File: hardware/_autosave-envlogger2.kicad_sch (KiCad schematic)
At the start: 20 parts, among them J1 Conn_01x06_Pin, J2 Conn_01x03_Socket, J3 Conn_01x03_Socket, SW1 SW_Push, U1 STM32L432KCUx, U2 BME280, Y1 32 kHz

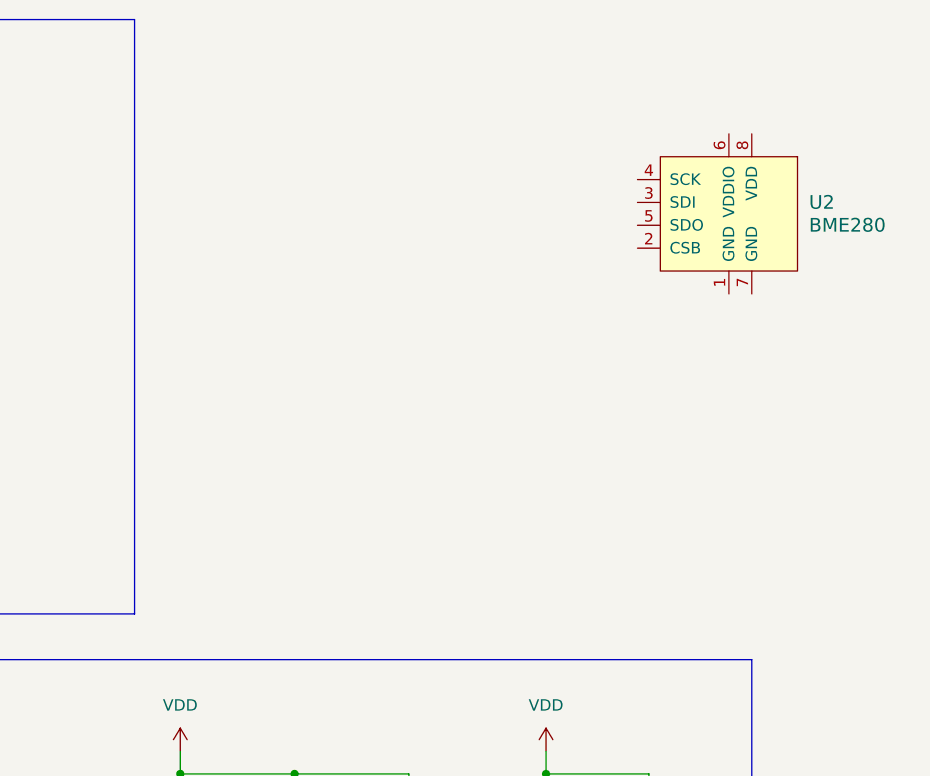
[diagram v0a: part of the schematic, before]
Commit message: Added BME280 schematic
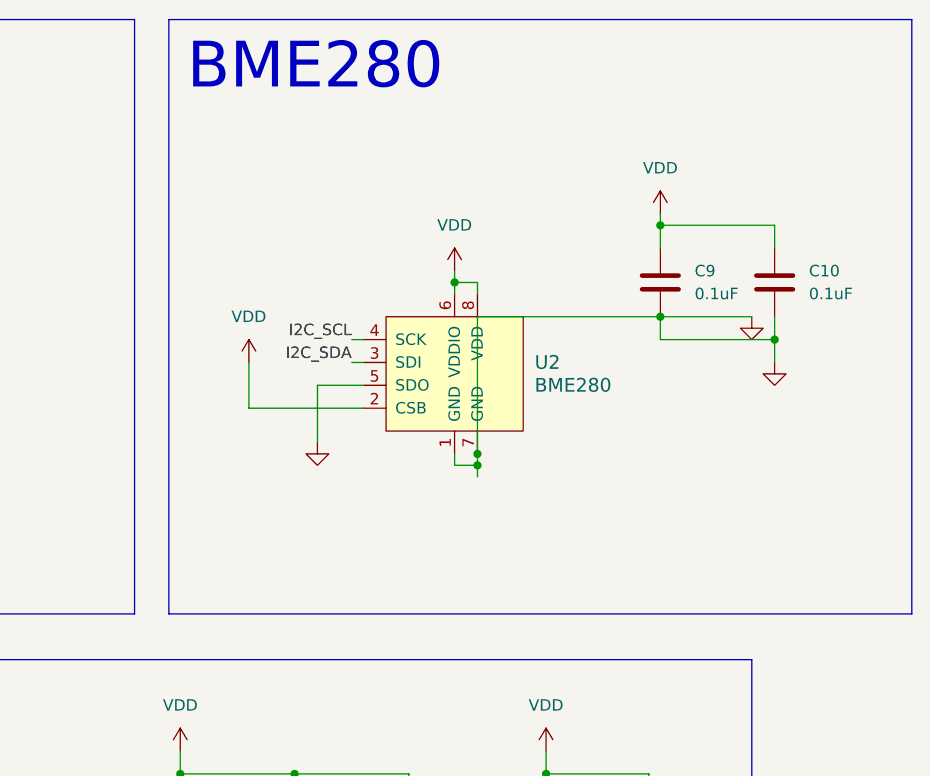
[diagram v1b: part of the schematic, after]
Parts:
- added C10, C9: 0.1uF, symbol Device:C
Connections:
- net GND: now also U2.1 (GND), U2.5 (SDO), U2.7 (GND), C10.2, C9.2
- net I2C_SCL: now also U2.4 (SCK)
- net I2C_SDA: now also U2.3 (SDI)
- net VDD: now also U2.2 (CSB), U2.6 (VDDIO), U2.8 (VDD), C10.1, C9.1
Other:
- note added: "BME280"
- moved on the sheet: U2
